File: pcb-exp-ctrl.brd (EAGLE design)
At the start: 100 x 80 mm, 15 parts, among them IC1 SAA1064, IC2 TINY13-20PU, T1 BC547, T2 BC547

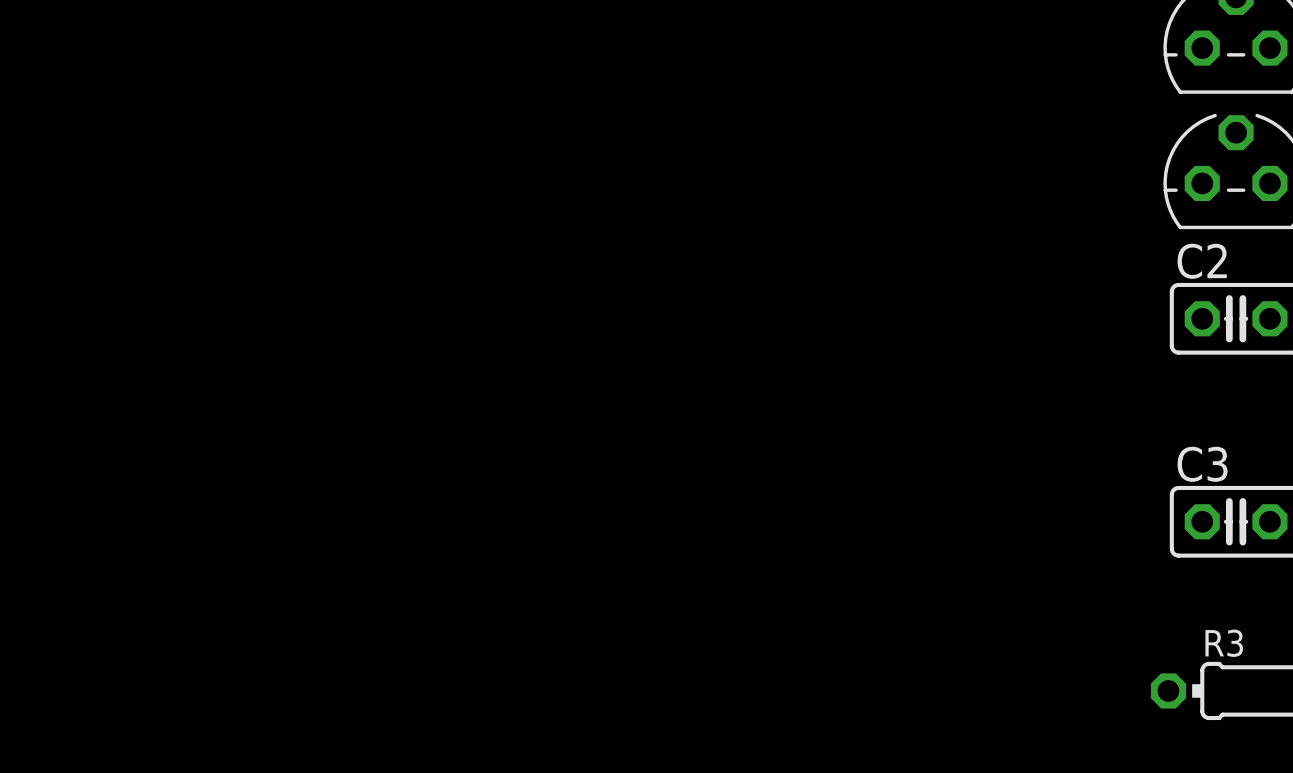
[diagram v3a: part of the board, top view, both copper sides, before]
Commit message: drei Taster nebst integrierten LEDs hinzugefügt und teilverdrahtet
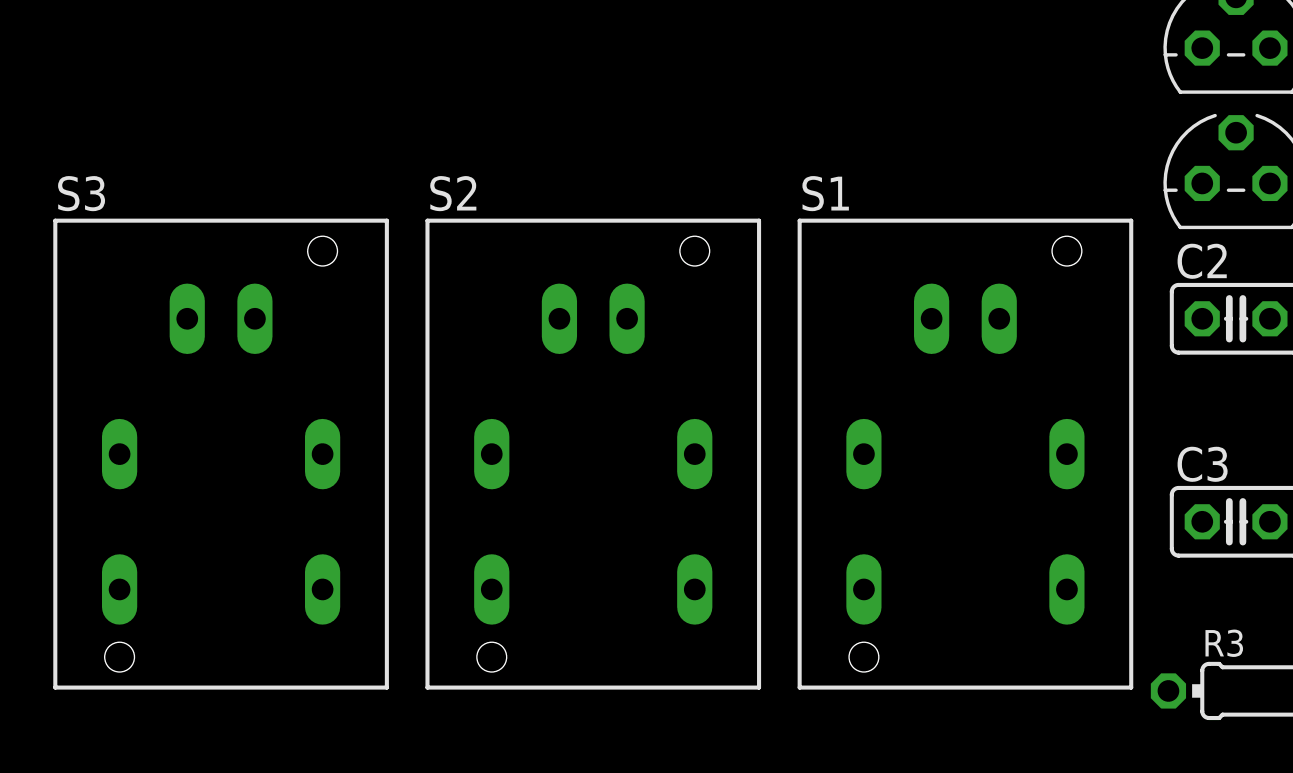
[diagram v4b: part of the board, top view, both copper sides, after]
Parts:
- added S1, S2, S3: SRKL, switch-misc:SRKL
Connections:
- net N$7: now also S1.-, S2.-, S3.-
- net P10: now also S2.+
- net P11: now also S3.+
- net P9: now also S1.+
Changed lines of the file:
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@@
 <attribute name="OC_FARNELL" value="unknown" x="40.64" y="8.89" size="1.778" layer="27" display="off"/>
 </element>
+<element name="S1" library="switch-misc" package="SRKL" value="SRKL" x="-6.35" y="-34.29"/>
+<element name="S2" library="switch-misc" package="SRKL" value="SRKL" x="-20.32" y="-34.29"/>
+<element name="S3" library="switch-misc" package="SRKL" value="SRKL" x="-34.29" y="-34.29"/>
 </elements>
 <signals>
@@
 <contactref element="IC1" pad="15"/>
 <contactref element="LED3" pad="7"/>
+<contactref element="S1" pad="+"/>
 <wire x1="27.94" y1="50.8" x2="38.1" y2="73.66" width="0" layer="19" extent="1-1"/>
+<wire x1="-7.62" y1="-29.21" x2="27.94" y2="50.8" width="0" layer="19" extent="1-1"/>
 </signal>
 <signal name="P10">
 <contactref element="IC1" pad="16"/>
 <contactref element="LED3" pad="6"/>
+<contactref element="S2" pad="+"/>
 <wire x1="25.4" y1="50.8" x2="40.64" y2="73.66" width="0" layer="19" extent="1-1"/>
+<wire x1="-21.59" y1="-29.21" x2="25.4" y2="50.8" width="0" layer="19" extent="1-1"/>
 </signal>
 <signal name="P11">
 <contactref element="IC1" pad="17"/>
 <contactref element="LED3" pad="4"/>
+<contactref element="S3" pad="+"/>
 <wire x1="22.86" y1="50.8" x2="38.1" y2="58.42" width="0" layer="19" extent="1-1"/>
+<wire x1="-35.56" y1="-29.21" x2="22.86" y2="50.8" width="0" layer="19" extent="1-1"/>
 </signal>
 <signal name="P12">
@@
 <contactref element="LED3" pad="3"/>
 <contactref element="T1" pad="1"/>
+<contactref element="S1" pad="-"/>
+<contactref element="S2" pad="-"/>
+<contactref element="S3" pad="-"/>
 <wire x1="35.56" y1="58.42" x2="35.56" y2="73.66" width="0" layer="19" extent="1-1"/>
 <wire x1="10.16" y1="73.66" x2="35.56" y2="73.66" width="0" layer="19" extent="1-1"/>
 <wire x1="10.16" y1="58.42" x2="10.16" y2="73.66" width="0" layer="19" extent="1-1"/>
 <wire x1="5.08" y1="-24.13" x2="10.16" y2="58.42" width="0" layer="19" extent="1-1"/>
+<wire x1="-5.08" y1="-29.21" x2="5.08" y2="-24.13" width="0" layer="19" extent="1-1"/>
+<wire x1="-19.05" y1="-29.21" x2="-5.08" y2="-29.21" width="0" layer="19" extent="1-1"/>
+<wire x1="-33.02" y1="-29.21" x2="-19.05" y2="-29.21" width="0" layer="19" extent="1-1"/>
 </signal>
 <signal name="N$8">

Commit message: spannungsregler nebst elko hinzugefügt
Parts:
- added C4: 2.2u, rcl:E2,5-6
- added IC3: LP2950Z, national-semiconductor:TO92
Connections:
- net +5V: now also C4.+, IC3.3
- net GND: now also C4.-, IC3.2
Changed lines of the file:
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@@
 <element name="S2" library="switch-misc" package="SRKL" value="SRKL" x="-20.32" y="-34.29"/>
 <element name="S3" library="switch-misc" package="SRKL" value="SRKL" x="-34.29" y="-34.29"/>
+<element name="IC3" library="national-semiconductor" package="TO92" value="LP2950Z" x="-38.1" y="-48.26">
+<attribute name="OC_NEWARK" value="41K6545" x="-38.1" y="-48.26" size="1.778" layer="27" display="off"/>
+<attribute name="MPN" value="LP2950CZ-5.0/NOPB" x="-38.1" y="-48.26" size="1.778" layer="27" display="off"/>
+<attribute name="MF" value="NATIONAL SEMICONDUCTOR" x="-38.1" y="-48.26" size="1.778" layer="27" display="off"/>
+<attribute name="OC_FARNELL" value="1150320" x="-38.1" y="-48.26" size="1.778" layer="27" display="off"/>
+</element>
+<element name="C4" library="rcl" package="E2,5-6" value="2.2u" x="-38.1" y="-53.34"/>
 </elements>
 <signals>
@@
 <contactref element="C3" pad="2"/>
 <contactref element="SV1" pad="6"/>
+<contactref element="IC3" pad="2"/>
+<contactref element="IC3" pad="2"/>
+<contactref element="C4" pad="-"/>
 <wire x1="40.894" y1="29.21" x2="45.72" y2="43.18" width="0" layer="19" extent="16-16"/>
 <wire x1="33.02" y1="35.56" x2="40.894" y2="29.21" width="0" layer="19" extent="16-16"/>
-<wire x1="5.08" y1="-12.7" x2="40.894" y2="29.21" width="0" layer="19" extent="16-16"/>
+<wire x1="43.18" y1="10.16" x2="40.894" y2="29.21" width="0" layer="19" extent="16-16"/>
+<wire x1="5.08" y1="-12.7" x2="43.18" y2="10.16" width="0" layer="19" extent="1-1"/>
 <wire x1="5.08" y1="-29.21" x2="5.08" y2="-12.7" width="0" layer="19" extent="1-1"/>
 <wire x1="5.08" y1="-36.83" x2="5.08" y2="-29.21" width="0" layer="19" extent="1-1"/>
-<wire x1="43.18" y1="10.16" x2="5.08" y2="-36.83" width="0" layer="19" extent="1-1"/>
+<wire x1="-38.1" y1="-46.355" x2="5.08" y2="-36.83" width="0" layer="19" extent="1-1"/>
+<wire x1="-36.83" y1="-53.34" x2="-38.1" y2="-46.355" width="0" layer="19" extent="1-1"/>
 </signal>
 <signal name="P1">
@@
 <wire x1="1.27" y1="-3.81" x2="7.62" y2="50.8" width="0" layer="19" extent="1-1"/>
 <wire x1="40.64" y1="10.16" x2="1.27" y2="-3.81" width="0" layer="19" extent="1-1"/>
-</signal>
-<signal name="+5V">
-<contactref element="IC2" pad="8"/>
-<contactref element="T2" pad="3"/>
-<contactref element="T1" pad="3"/>
-<contactref element="C2" pad="1"/>
-<contactref element="R1" pad="2"/>
-<contactref element="R2" pad="2"/>
-<contactref element="IC1" pad="13"/>
-<contactref element="SJ1" pad="3"/>
-<contactref element="C3" pad="1"/>
-<contactref element="R3" pad="2"/>
-<contactref element="SV1" pad="2"/>
-<wire x1="33.02" y1="50.8" x2="38.1" y2="50.8" width="0" layer="19" extent="1-1"/>
-<wire x1="37.846" y1="29.21" x2="38.1" y2="50.8" width="0" layer="19" extent="16-16"/>
-<wire x1="8.89" y1="-3.81" x2="37.846" y2="29.21" width="0" layer="19" extent="16-16"/>
-<wire x1="8.89" y1="-7.62" x2="8.89" y2="-3.81" width="0" layer="19" extent="1-1"/>
-<wire x1="2.54" y1="-19.05" x2="8.89" y2="-7.62" width="0" layer="19" extent="1-1"/>
-<wire x1="2.54" y1="-24.13" x2="2.54" y2="-19.05" width="0" layer="19" extent="1-1"/>
-<wire x1="2.54" y1="-29.21" x2="2.54" y2="-24.13" width="0" layer="19" extent="1-1"/>
-<wire x1="2.54" y1="-36.83" x2="2.54" y2="-29.21" width="0" layer="19" extent="1-1"/>
-<wire x1="8.89" y1="-43.18" x2="2.54" y2="-36.83" width="0" layer="19" extent="1-1"/>
-<wire x1="38.1" y1="10.16" x2="8.89" y2="-43.18" width="0" layer="19" extent="1-1"/>
 </signal>
 <signal name="N$6">
@@
 <wire x1="38.1" y1="7.62" x2="43.18" y2="50.8" width="0" layer="19" extent="1-1"/>
 </signal>
+<signal name="+5V">
+<contactref element="T2" pad="3"/>
+<contactref element="T1" pad="3"/>
+<contactref element="C2" pad="1"/>
+<contactref element="R1" pad="2"/>
+<contactref element="R2" pad="2"/>
+<contactref element="IC1" pad="13"/>
+<contactref element="SJ1" pad="3"/>
+<contactref element="SV1" pad="2"/>
+<contactref element="IC3" pad="3"/>
+<contactref element="IC2" pad="8"/>
+<contactref element="C3" pad="1"/>
+<contactref element="R3" pad="2"/>
+<contactref element="C4" pad="+"/>
+<wire x1="-36.83" y1="-48.26" x2="-39.37" y2="-53.34" width="0" layer="19" extent="1-1"/>
+<wire x1="2.54" y1="-36.83" x2="-36.83" y2="-48.26" width="0" layer="19" extent="1-1"/>
+<wire x1="2.54" y1="-29.21" x2="2.54" y2="-36.83" width="0" layer="19" extent="1-1"/>
+<wire x1="2.54" y1="-24.13" x2="2.54" y2="-29.21" width="0" layer="19" extent="1-1"/>
+<wire x1="2.54" y1="-19.05" x2="2.54" y2="-24.13" width="0" layer="19" extent="1-1"/>
+<wire x1="8.89" y1="-43.18" x2="2.54" y2="-36.83" width="0" layer="19" extent="1-1"/>
+<wire x1="8.89" y1="-7.62" x2="2.54" y2="-19.05" width="0" layer="19" extent="1-1"/>
+<wire x1="8.89" y1="-3.81" x2="8.89" y2="-7.62" width="0" layer="19" extent="1-1"/>
+<wire x1="38.1" y1="10.16" x2="8.89" y2="-3.81" width="0" layer="19" extent="1-1"/>
+<wire x1="37.846" y1="29.21" x2="38.1" y2="10.16" width="0" layer="19" extent="16-16"/>
+<wire x1="38.1" y1="50.8" x2="37.846" y2="29.21" width="0" layer="19" extent="16-16"/>
+<wire x1="33.02" y1="50.8" x2="38.1" y2="50.8" width="0" layer="19" extent="1-1"/>
+</signal>
 </signals>

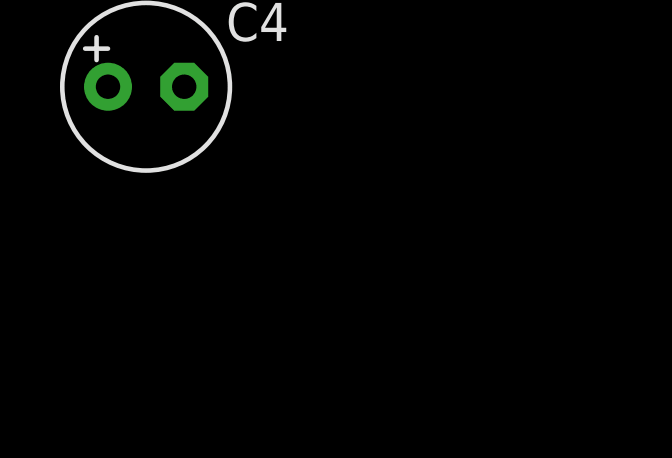
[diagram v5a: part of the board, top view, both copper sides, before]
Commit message: add NPN for switching UV LEDs
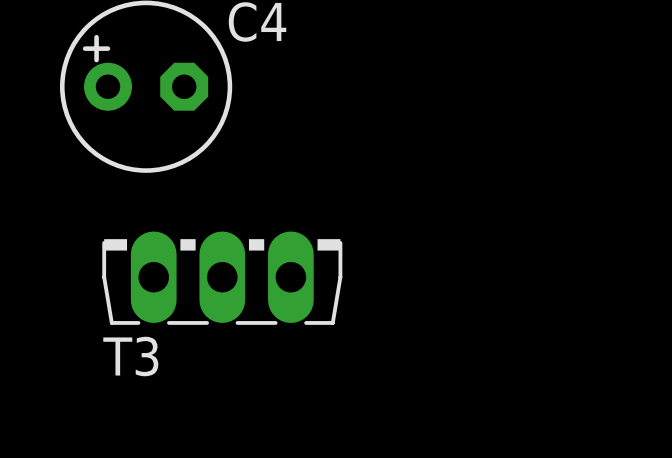
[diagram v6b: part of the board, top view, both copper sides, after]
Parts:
- added T3: BD131, transistor:TO126V
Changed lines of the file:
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@@
 </element>
 <element name="C4" library="rcl" package="E2,5-6" value="2.2u" x="-38.1" y="-53.34"/>
+<element name="T3" library="transistor" package="TO126V" value="BD131" x="-35.56" y="-58.42"/>
 </elements>
 <signals>

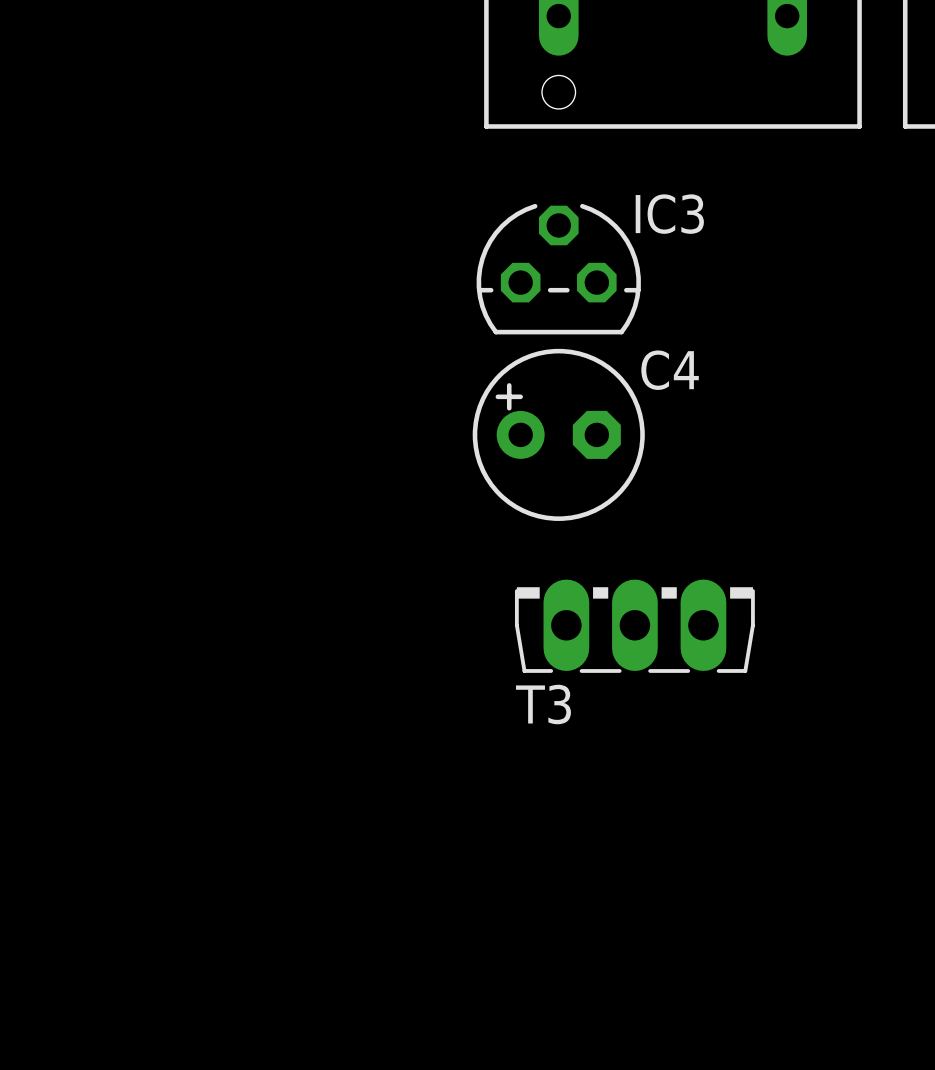
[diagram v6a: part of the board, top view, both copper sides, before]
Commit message: replace NPN with relay
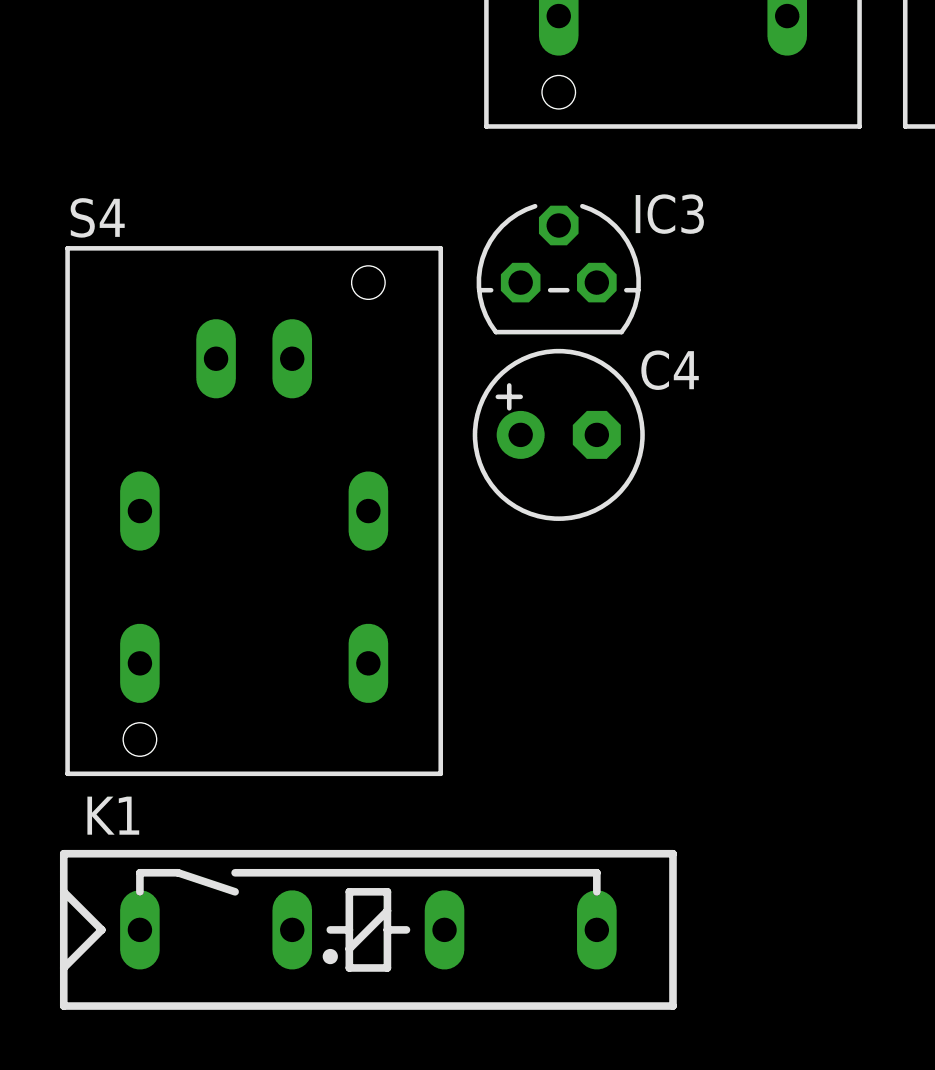
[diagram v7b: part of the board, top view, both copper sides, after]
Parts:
- removed T3: BD131, transistor:TO126V
- added K1: REED, relay:REED
- added S4: SRKL, switch-misc:SRKL
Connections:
- net GND: now also K1.1, K1.5
- net MISO: now also K1.3
- net N$7: now also S4.-
- net P12: now also S4.+
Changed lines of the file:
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@@
 </element>
 <element name="C4" library="rcl" package="E2,5-6" value="2.2u" x="-38.1" y="-53.34"/>
-<element name="T3" library="transistor" package="TO126V" value="BD131" x="-35.56" y="-58.42"/>
+<element name="S4" library="switch-misc" package="SRKL" value="SRKL" x="-48.26" y="-55.88"/>
+<element name="K1" library="relay" package="REED" value="REED" x="-34.29" y="-72.39">
+<attribute name="OC_NEWARK" value="unknown" x="-34.29" y="-72.39" size="1.778" layer="27" display="off"/>
+<attribute name="MPN" value="" x="-34.29" y="-72.39" size="1.778" layer="27" display="off"/>
+<attribute name="MF" value="" x="-34.29" y="-72.39" size="1.778" layer="27" display="off"/>
+<attribute name="OC_FARNELL" value="unknown" x="-34.29" y="-72.39" size="1.778" layer="27" display="off"/>
+</element>
 </elements>
 <signals>
@@
 <contactref element="IC3" pad="2"/>
 <contactref element="C4" pad="-"/>
-<wire x1="40.894" y1="29.21" x2="45.72" y2="43.18" width="0" layer="19" extent="16-16"/>
+<contactref element="K1" pad="5"/>
+<contactref element="K1" pad="1"/>
+<wire x1="-41.91" y1="-69.85" x2="-52.07" y2="-69.85" width="0" layer="19" extent="1-1"/>
+<wire x1="-36.83" y1="-53.34" x2="-41.91" y2="-69.85" width="0" layer="19" extent="1-1"/>
+<wire x1="-38.1" y1="-46.355" x2="-36.83" y2="-53.34" width="0" layer="19" extent="1-1"/>
+<wire x1="5.08" y1="-36.83" x2="-38.1" y2="-46.355" width="0" layer="19" extent="1-1"/>
+<wire x1="5.08" y1="-29.21" x2="5.08" y2="-36.83" width="0" layer="19" extent="1-1"/>
+<wire x1="5.08" y1="-12.7" x2="5.08" y2="-29.21" width="0" layer="19" extent="1-1"/>
+<wire x1="43.18" y1="10.16" x2="5.08" y2="-12.7" width="0" layer="19" extent="1-1"/>
+<wire x1="40.894" y1="29.21" x2="43.18" y2="10.16" width="0" layer="19" extent="16-16"/>
 <wire x1="33.02" y1="35.56" x2="40.894" y2="29.21" width="0" layer="19" extent="16-16"/>
-<wire x1="43.18" y1="10.16" x2="40.894" y2="29.21" width="0" layer="19" extent="16-16"/>
-<wire x1="5.08" y1="-12.7" x2="43.18" y2="10.16" width="0" layer="19" extent="1-1"/>
-<wire x1="5.08" y1="-29.21" x2="5.08" y2="-12.7" width="0" layer="19" extent="1-1"/>
-<wire x1="5.08" y1="-36.83" x2="5.08" y2="-29.21" width="0" layer="19" extent="1-1"/>
-<wire x1="-38.1" y1="-46.355" x2="5.08" y2="-36.83" width="0" layer="19" extent="1-1"/>
-<wire x1="-36.83" y1="-53.34" x2="-38.1" y2="-46.355" width="0" layer="19" extent="1-1"/>
+<wire x1="45.72" y1="43.18" x2="40.894" y2="29.21" width="0" layer="19" extent="16-16"/>
 </signal>
 <signal name="P1">
@@
 <contactref element="IC1" pad="18"/>
 <contactref element="LED3" pad="2"/>
-<wire x1="20.32" y1="50.8" x2="33.02" y2="58.42" width="0" layer="19" extent="1-1"/>
+<contactref element="S4" pad="+"/>
+<wire x1="20.32" y1="50.8" x2="-49.53" y2="-50.8" width="0" layer="19" extent="1-1"/>
+<wire x1="33.02" y1="58.42" x2="20.32" y2="50.8" width="0" layer="19" extent="1-1"/>
 </signal>
 <signal name="P13">
@@
 <contactref element="S2" pad="-"/>
 <contactref element="S3" pad="-"/>
+<contactref element="S4" pad="-"/>
 <wire x1="35.56" y1="58.42" x2="35.56" y2="73.66" width="0" layer="19" extent="1-1"/>
 <wire x1="10.16" y1="73.66" x2="35.56" y2="73.66" width="0" layer="19" extent="1-1"/>
@@
 <wire x1="-19.05" y1="-29.21" x2="-5.08" y2="-29.21" width="0" layer="19" extent="1-1"/>
 <wire x1="-33.02" y1="-29.21" x2="-19.05" y2="-29.21" width="0" layer="19" extent="1-1"/>
+<wire x1="-46.99" y1="-50.8" x2="-33.02" y2="-29.21" width="0" layer="19" extent="1-1"/>
 </signal>
 <signal name="N$8">
@@
 <contactref element="IC2" pad="6"/>
 <contactref element="SV1" pad="1"/>
-<wire x1="38.1" y1="7.62" x2="43.18" y2="50.8" width="0" layer="19" extent="1-1"/>
+<contactref element="K1" pad="3"/>
+<wire x1="38.1" y1="7.62" x2="-46.99" y2="-69.85" width="0" layer="19" extent="1-1"/>
+<wire x1="43.18" y1="50.8" x2="38.1" y2="7.62" width="0" layer="19" extent="1-1"/>
 </signal>
 <signal name="+5V">
